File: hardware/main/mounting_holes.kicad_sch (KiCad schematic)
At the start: 8 parts

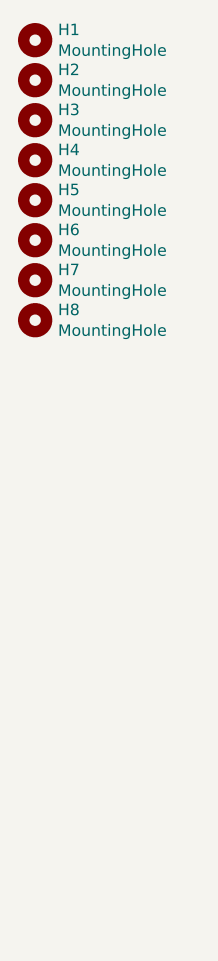
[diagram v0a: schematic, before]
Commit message: Main: Add mounting holes
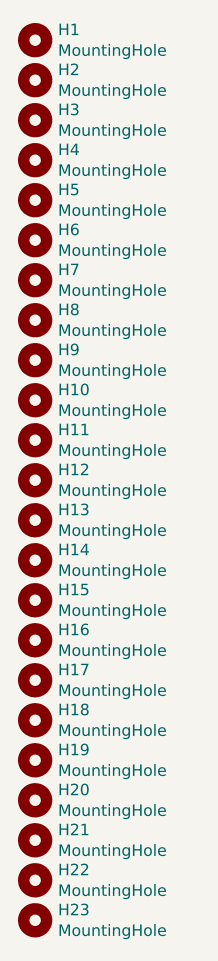
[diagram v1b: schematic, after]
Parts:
- added H10, H11, H12, H13, H14, H15, H16, H17, H18, H19, H20, H21, H22, H23, H9: MountingHole, MountingHole:MountingHole_2.2mm_M2_Pad, symbol Mechanical:MountingHole
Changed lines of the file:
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@@
+    )
+  )
+  (symbol (lib_id "Mechanical:MountingHole") (at 32.385 71.12 0) (unit 1)
+    (in_bom yes) (on_board yes)
+    (property "Reference" "H9" (id 0) (at 34.9251 69.9706 0)
+      (effects (font (size 1.27 1.27)) (justify left))
+    )
+    (property "Value" "MountingHole" (id 1) (at 34.9251 72.2693 0)
+      (effects (font (size 1.27 1.27)) (justify left))
+    )
+    (property "Footprint" "MountingHole:MountingHole_2.2mm_M2_Pad" (id 2) (at 32.385 71.12 0)
+      (effects (font (size 1.27 1.27)) hide)
+    )
+    (property "Datasheet" "~" (id 3) (at 32.385 71.12 0)
+      (effects (font (size 1.27 1.27)) hide)
+    )
+  )
+  (symbol (lib_id "Mechanical:MountingHole") (at 32.385 75.565 0) (unit 1)
+    (in_bom yes) (on_board yes)
+    (property "Reference" "H10" (id 0) (at 34.9251 74.4156 0)
+      (effects (font (size 1.27 1.27)) (justify left))
+    )
+    (property "Value" "MountingHole" (id 1) (at 34.9251 76.7143 0)
+      (effects (font (size 1.27 1.27)) (justify left))
+    )
+    (property "Footprint" "MountingHole:MountingHole_2.2mm_M2_Pad" (id 2) (at 32.385 75.565 0)
+      (effects (font (size 1.27 1.27)) hide)
+    )
+    (property "Datasheet" "~" (id 3) (at 32.385 75.565 0)
+      (effects (font (size 1.27 1.27)) hide)
+    )
+  )
+  (symbol (lib_id "Mechanical:MountingHole") (at 32.385 80.01 0) (unit 1)
+    (in_bom yes) (on_board yes)
+    (property "Reference" "H11" (id 0) (at 34.9251 78.8606 0)
+      (effects (font (size 1.27 1.27)) (justify left))
+    )
+    (property "Value" "MountingHole" (id 1) (at 34.9251 81.1593 0)
+      (effects (font (size 1.27 1.27)) (justify left))
+    )
+    (property "Footprint" "MountingHole:MountingHole_2.2mm_M2_Pad" (id 2) (at 32.385 80.01 0)
+      (effects (font (size 1.27 1.27)) hide)
+    )
+    (property "Datasheet" "~" (id 3) (at 32.385 80.01 0)
+      (effects (font (size 1.27 1.27)) hide)
+    )
+  )
+  (symbol (lib_id "Mechanical:MountingHole") (at 32.385 84.455 0) (unit 1)
+    (in_bom yes) (on_board yes)
+    (property "Reference" "H12" (id 0) (at 34.9251 83.3056 0)
+      (effects (font (size 1.27 1.27)) (justify left))
+    )
+    (property "Value" "MountingHole" (id 1) (at 34.9251 85.6043 0)
+      (effects (font (size 1.27 1.27)) (justify left))
+    )
+    (property "Footprint" "MountingHole:MountingHole_2.2mm_M2_Pad" (id 2) (at 32.385 84.455 0)
+      (effects (font (size 1.27 1.27)) hide)
+    )
+    (property "Datasheet" "~" (id 3) (at 32.385 84.455 0)
+      (effects (font (size 1.27 1.27)) hide)
+    )
+  )
+  (symbol (lib_id "Mechanical:MountingHole") (at 32.385 88.9 0) (unit 1)
+    (in_bom yes) (on_board yes)
+    (property "Reference" "H13" (id 0) (at 34.9251 87.7506 0)
+      (effects (font (size 1.27 1.27)) (justify left))
+    )
+    (property "Value" "MountingHole" (id 1) (at 34.9251 90.0493 0)
+      (effects (font (size 1.27 1.27)) (justify left))
+    )
+    (property "Footprint" "MountingHole:MountingHole_2.2mm_M2_Pad" (id 2) (at 32.385 88.9 0)
+      (effects (font (size 1.27 1.27)) hide)
+    )
+    (property "Datasheet" "~" (id 3) (at 32.385 88.9 0)
+      (effects (font (size 1.27 1.27)) hide)
+    )
+  )
+  (symbol (lib_id "Mechanical:MountingHole") (at 32.385 93.345 0) (unit 1)
+    (in_bom yes) (on_board yes)
+    (property "Reference" "H14" (id 0) (at 34.9251 92.1956 0)
+      (effects (font (size 1.27 1.27)) (justify left))
+    )
+    (property "Value" "MountingHole" (id 1) (at 34.9251 94.4943 0)
+      (effects (font (size 1.27 1.27)) (justify left))
+    )
+    (property "Footprint" "MountingHole:MountingHole_2.2mm_M2_Pad" (id 2) (at 32.385 93.345 0)
+      (effects (font (size 1.27 1.27)) hide)
+    )
+    (property "Datasheet" "~" (id 3) (at 32.385 93.345 0)
+      (effects (font (size 1.27 1.27)) hide)
+    )
+  )
+  (symbol (lib_id "Mechanical:MountingHole") (at 32.385 97.79 0) (unit 1)
+    (in_bom yes) (on_board yes)
+    (property "Reference" "H15" (id 0) (at 34.9251 96.6406 0)
+      (effects (font (size 1.27 1.27)) (justify left))
+    )
+    (property "Value" "MountingHole" (id 1) (at 34.9251 98.9393 0)
+      (effects (font (size 1.27 1.27)) (justify left))
+    )
+    (property "Footprint" "MountingHole:MountingHole_2.2mm_M2_Pad" (id 2) (at 32.385 97.79 0)
+      (effects (font (size 1.27 1.27)) hide)
+    )
+    (property "Datasheet" "~" (id 3) (at 32.385 97.79 0)
+      (effects (font (size 1.27 1.27)) hide)
+    )
+  )
+  (symbol (lib_id "Mechanical:MountingHole") (at 32.385 102.235 0) (unit 1)
+    (in_bom yes) (on_board yes)
+    (property "Reference" "H16" (id 0) (at 34.9251 101.0856 0)
+      (effects (font (size 1.27 1.27)) (justify left))
+    )
+    (property "Value" "MountingHole" (id 1) (at 34.9251 103.3843 0)
+      (effects (font (size 1.27 1.27)) (justify left))
+    )
+    (property "Footprint" "MountingHole:MountingHole_2.2mm_M2_Pad" (id 2) (at 32.385 102.235 0)
+      (effects (font (size 1.27 1.27)) hide)
+    )
+    (property "Datasheet" "~" (id 3) (at 32.385 102.235 0)
+      (effects (font (size 1.27 1.27)) hide)
+    )
+  )
+  (symbol (lib_id "Mechanical:MountingHole") (at 32.385 106.68 0) (unit 1)
+    (in_bom yes) (on_board yes)
+    (property "Reference" "H17" (id 0) (at 34.9251 105.5306 0)
+      (effects (font (size 1.27 1.27)) (justify left))
+    )
+    (property "Value" "MountingHole" (id 1) (at 34.9251 107.8293 0)
+      (effects (font (size 1.27 1.27)) (justify left))
+    )
+    (property "Footprint" "MountingHole:MountingHole_2.2mm_M2_Pad" (id 2) (at 32.385 106.68 0)
+      (effects (font (size 1.27 1.27)) hide)
+    )
+    (property "Datasheet" "~" (id 3) (at 32.385 106.68 0)
+      (effects (font (size 1.27 1.27)) hide)
+    )
+  )
+  (symbol (lib_id "Mechanical:MountingHole") (at 32.385 111.125 0) (unit 1)
+    (in_bom yes) (on_board yes)
+    (property "Reference" "H18" (id 0) (at 34.9251 109.9756 0)
+      (effects (font (size 1.27 1.27)) (justify left))
+    )
+    (property "Value" "MountingHole" (id 1) (at 34.9251 112.2743 0)
+      (effects (font (size 1.27 1.27)) (justify left))
+    )
+    (property "Footprint" "MountingHole:MountingHole_2.2mm_M2_Pad" (id 2) (at 32.385 111.125 0)
+      (effects (font (size 1.27 1.27)) hide)
+    )
+    (property "Datasheet" "~" (id 3) (at 32.385 111.125 0)
+      (effects (font (size 1.27 1.27)) hide)
+    )
+  )
+  (symbol (lib_id "Mechanical:MountingHole") (at 32.385 115.57 0) (unit 1)
+    (in_bom yes) (on_board yes)
+    (property "Reference" "H19" (id 0) (at 34.9251 114.4206 0)
+      (effects (font (size 1.27 1.27)) (justify left))
+    )
+    (property "Value" "MountingHole" (id 1) (at 34.9251 116.7193 0)
+      (effects (font (size 1.27 1.27)) (justify left))
+    )
+    (property "Footprint" "MountingHole:MountingHole_2.2mm_M2_Pad" (id 2) (at 32.385 115.57 0)
+      (effects (font (size 1.27 1.27)) hide)
+    )
+    (property "Datasheet" "~" (id 3) (at 32.385 115.57 0)
+      (effects (font (size 1.27 1.27)) hide)
+    )
+  )
+  (symbol (lib_id "Mechanical:MountingHole") (at 32.385 120.015 0) (unit 1)
+    (in_bom yes) (on_board yes)
+    (property "Reference" "H20" (id 0) (at 34.9251 118.8656 0)
+      (effects (font (size 1.27 1.27)) (justify left))
+    )
+    (property "Value" "MountingHole" (id 1) (at 34.9251 121.1643 0)
+      (effects (font (size 1.27 1.27)) (justify left))
+    )
+    (property "Footprint" "MountingHole:MountingHole_2.2mm_M2_Pad" (id 2) (at 32.385 120.015 0)
+      (effects (font (size 1.27 1.27)) hide)
+    )
+    (property "Datasheet" "~" (id 3) (at 32.385 120.015 0)
+      (effects (font (size 1.27 1.27)) hide)
+    )
+  )
+  (symbol (lib_id "Mechanical:MountingHole") (at 32.385 124.46 0) (unit 1)
+    (in_bom yes) (on_board yes)
+    (property "Reference" "H21" (id 0) (at 34.9251 123.3106 0)
+      (effects (font (size 1.27 1.27)) (justify left))
+    )
+    (property "Value" "MountingHole" (id 1) (at 34.9251 125.6093 0)
+      (effects (font (size 1.27 1.27)) (justify left))
+    )
+    (property "Footprint" "MountingHole:MountingHole_2.2mm_M2_Pad" (id 2) (at 32.385 124.46 0)
+      (effects (font (size 1.27 1.27)) hide)
+    )
+    (property "Datasheet" "~" (id 3) (at 32.385 124.46 0)
+      (effects (font (size 1.27 1.27)) hide)
+    )
+  )
+  (symbol (lib_id "Mechanical:MountingHole") (at 32.385 128.905 0) (unit 1)
+    (in_bom yes) (on_board yes)
+    (property "Reference" "H22" (id 0) (at 34.9251 127.7556 0)
+      (effects (font (size 1.27 1.27)) (justify left))
+    )
+    (property "Value" "MountingHole" (id 1) (at 34.9251 130.0543 0)
+      (effects (font (size 1.27 1.27)) (justify left))
+    )
+    (property "Footprint" "MountingHole:MountingHole_2.2mm_M2_Pad" (id 2) (at 32.385 128.905 0)
+      (effects (font (size 1.27 1.27)) hide)
+    )
+    (property "Datasheet" "~" (id 3) (at 32.385 128.905 0)
+      (effects (font (size 1.27 1.27)) hide)
+    )
+  )
+  (symbol (lib_id "Mechanical:MountingHole") (at 32.385 133.35 0) (unit 1)
+    (in_bom yes) (on_board yes)
+    (property "Reference" "H23" (id 0) (at 34.9251 132.2006 0)
+      (effects (font (size 1.27 1.27)) (justify left))
+    )
+    (property "Value" "MountingHole" (id 1) (at 34.9251 134.4993 0)
+      (effects (font (size 1.27 1.27)) (justify left))
+    )
+    (property "Footprint" "MountingHole:MountingHole_2.2mm_M2_Pad" (id 2) (at 32.385 133.35 0)
+      (effects (font (size 1.27 1.27)) hide)
+    )
+    (property "Datasheet" "~" (id 3) (at 32.385 133.35 0)
+      (effects (font (size 1.27 1.27)) hide)
     )
   )
